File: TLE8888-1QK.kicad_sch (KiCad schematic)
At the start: 40 parts, among them J15 Conn_01x01, J17 Conn_01x01, Q1 IPD30N06S2L-23, U2 TLE8888QK

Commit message: KiCAD6 version
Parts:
- added JP4, JP5: (no value), symbol Jumper:SolderJumper_2_Open
- R17, R18, R19: value DNP -> (none)
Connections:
- net CRNK+: now also JP5.1 (A); no longer R17.2
- net CRNK-: now also JP4.1 (A); no longer R18.2, R19.2
- new net: JP5.2 (B), R17.2
- new net: JP4.2 (B), R18.2, R19.2
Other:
- moved on the sheet: R17

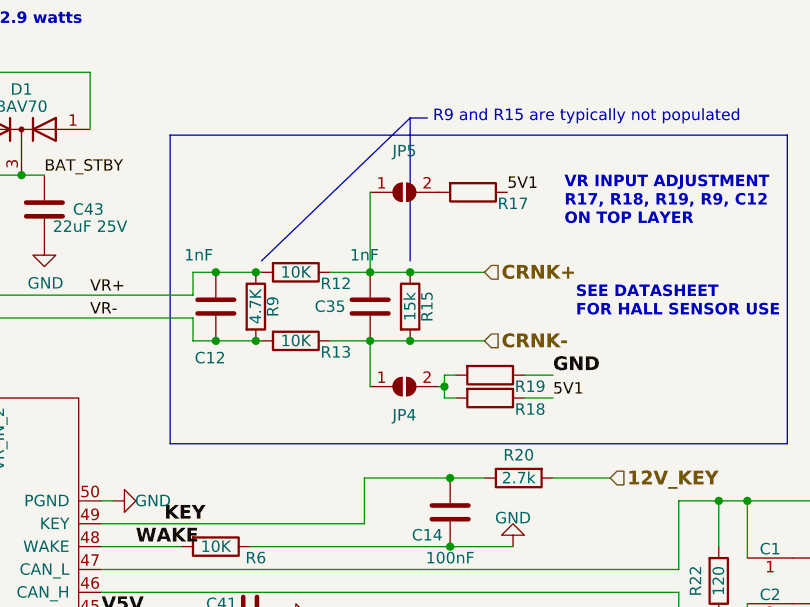
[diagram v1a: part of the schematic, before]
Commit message: R15 set as DNP
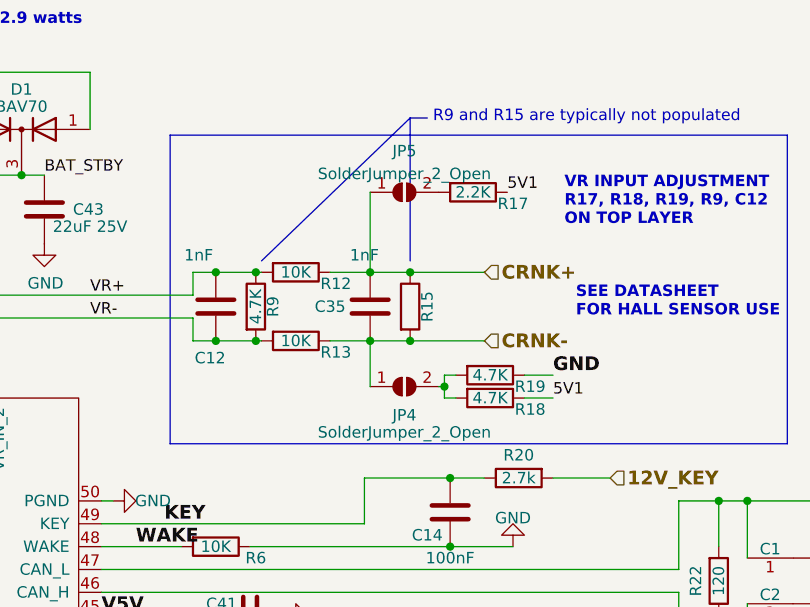
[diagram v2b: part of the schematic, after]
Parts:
- JP4, JP5: value (none) -> SolderJumper_2_Open; footprint (none) -> Jumper:SolderJumper-2_P1.3mm_Open_RoundedPad1.0x1.5mm
- R15: value 15k -> (none)
- R17: value (none) -> 2.2K
- R18, R19: value (none) -> 4.7K

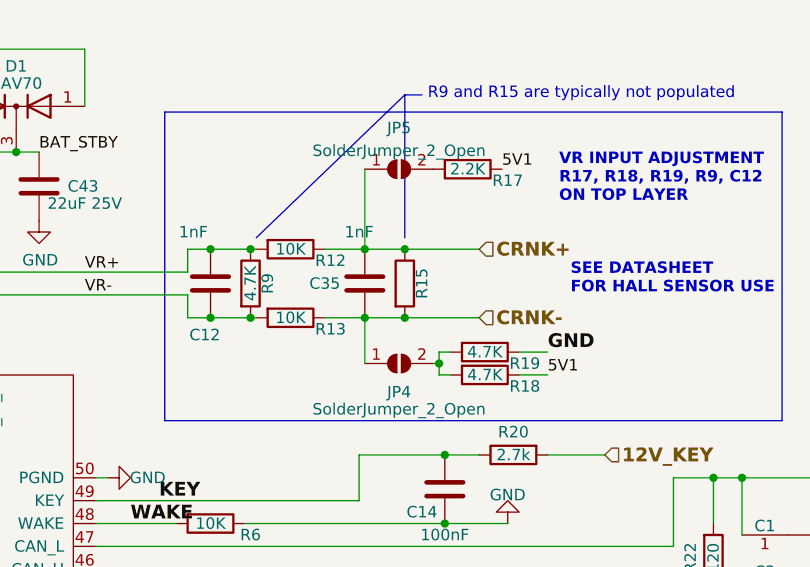
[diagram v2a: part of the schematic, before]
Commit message: Dual footprint for SDCard - SPI2 & SPI3
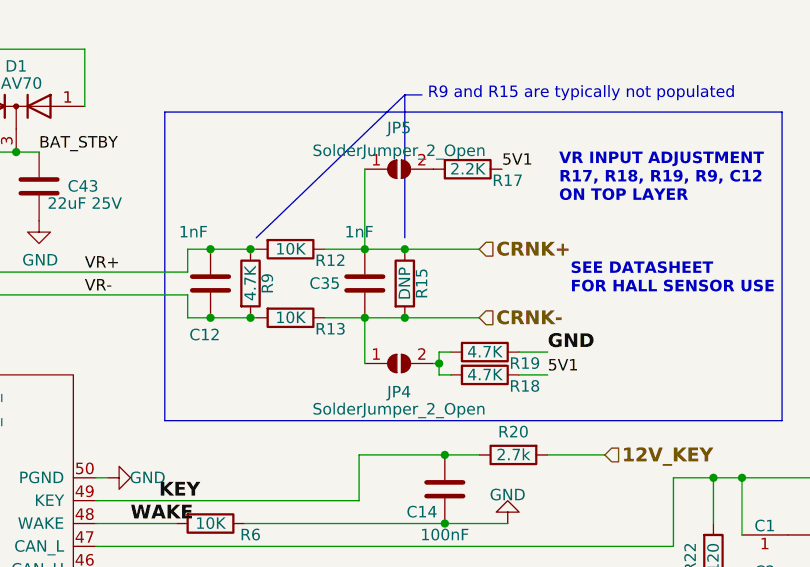
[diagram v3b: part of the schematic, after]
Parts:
- R15: value (none) -> DNP
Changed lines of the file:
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@@
     (in_bom yes) (on_board yes)
     (property "Reference" "R15" (id 0) (at 328.295 162.56 90))
-    (property "Value" "" (id 1) (at 326.39 162.56 90))
+    (property "Value" "DNP" (id 1) (at 326.39 162.56 90))
     (property "Footprint" "Resistor_SMD:R_0603_1608Metric" (id 2) (at 324.612 162.56 90)
       (effects (font (size 1.27 1.27)) hide)

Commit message: R0.6.1rc KICAD6
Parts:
- R3: footprint Resistor_SMD:R_0805_2012Metric -> Resistor_SMD:R_0603_1608Metric
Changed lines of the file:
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@@
     (property "Reference" "R3" (id 0) (at 193.04 262.89 90))
     (property "Value" "10K" (id 1) (at 188.595 261.62 90))
-    (property "Footprint" "Resistor_SMD:R_0805_2012Metric" (id 2) (at 188.595 259.842 90)
+    (property "Footprint" "Resistor_SMD:R_0603_1608Metric" (id 2) (at 188.595 259.842 90)
       (effects (font (size 1.27 1.27)) hide)
     )
